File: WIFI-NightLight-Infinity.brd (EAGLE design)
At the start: 49.2 x 44.4 mm, 34 parts, among them CN1 PBS-3-VERTICAL, CN2 PBS-2-VERTICAL, CN5 PBS-2-VERTICAL, CN6 PBS-2-VERTICAL, CN7 PBS-4-VERTICAL, IC3 MC34063AD, IC4 DS1307Z, M1 ESP8266-12F, Q1 32.768K

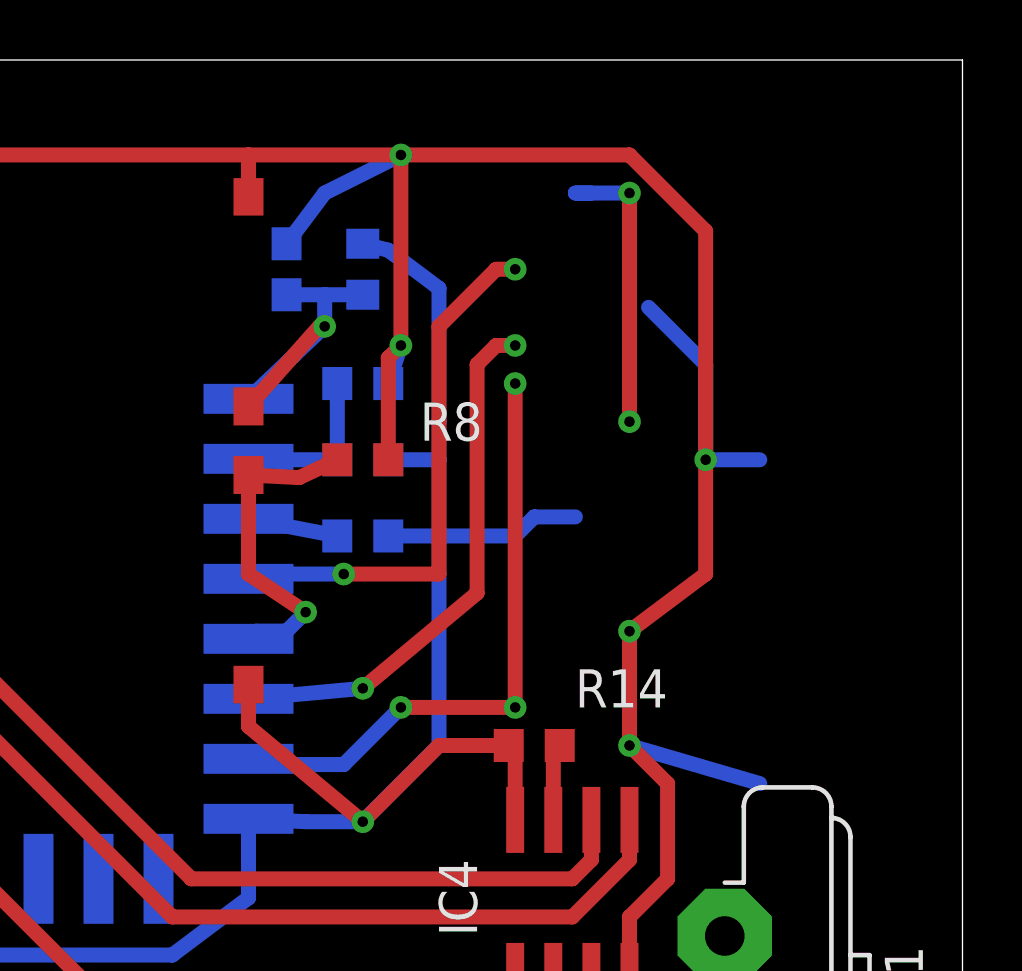
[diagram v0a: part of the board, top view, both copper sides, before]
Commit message: transistors were aaded
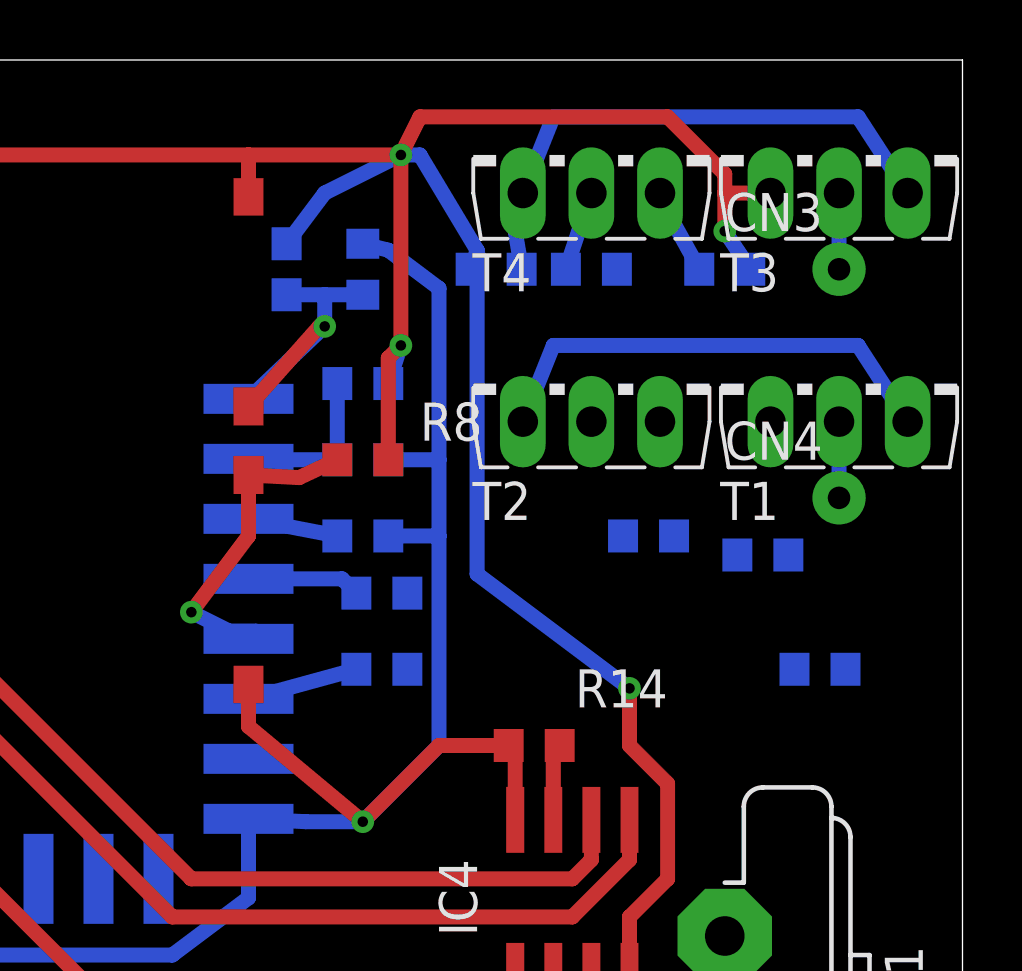
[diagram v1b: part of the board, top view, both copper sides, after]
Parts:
- added CN3, CN4: (no value), pls:PBS-1-VERTICAL
- added R15, R16, R17, R18, R19, R20, R21, R22: 100K, eagle-ltspice:R0603
- added T1, T2, T3, T4: (no value), transistor:TO126V
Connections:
- net SCK renamed LED_KEY_B
- removed net N$27: M1.G16
- removed net RCK: M1.G12
- new net LED_KEY_G: M1.G12, R19.2
- new net LED_KEY_R: M1.G16, R15.2
- new net N$10: R17.1, T4.2
- new net N$11: R19.1, R20.2, T2.3
- new net N$12: CN3.P$1, T3.2
- new net N$13: R21.2, T1.3, T2.1
- new net N$14: R22.1, T2.2
- new net N$15: CN4.P$1, T1.2
- new net N$8: R15.1, R18.2, T4.3
- new net N$9: R16.2, T3.3, T4.1
- net +5V: now also R17.2, R22.2
- net GND: now also R16.1, R18.1, R20.1, R21.1, T1.1, T3.1
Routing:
- net LED_KEY_B: track 20.5 -> 0.00 mm, vias 3 -> 0
- net N$9: track 0.00 -> 18.5 mm
- net N$27: track 18.0 -> 0.00 mm, vias 2 -> 0
- net RCK: track 17.9 -> 0.00 mm, vias 2 -> 0
- net N$13: track 0.00 -> 15.9 mm
- net +3V3: track 135.1 -> 120.4 mm, vias 5 -> 3
- net LED_KEY_R: track 0.00 -> 3.79 mm
- net LED_KEY_G: track 0.00 -> 3.73 mm
- net N$8: track 0.00 -> 3.46 mm
- net N$10: track 0.00 -> 2.68 mm
- net N$15: track 0.00 -> 2.54 mm
- net N$12: track 0.00 -> 2.54 mm
- net GND: track 262.9 -> 262.5 mm, vias 9 -> 8
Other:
- board text added: "Polyakov Konstantin Russia, Yeysk, 2018-09-16, v0.1 rev1"
- board text removed: "16 Channels 1"
- board text removed: "Polyakov Konstantin Russia, Yeysk, 2018-04-26, v0.3 rev1"

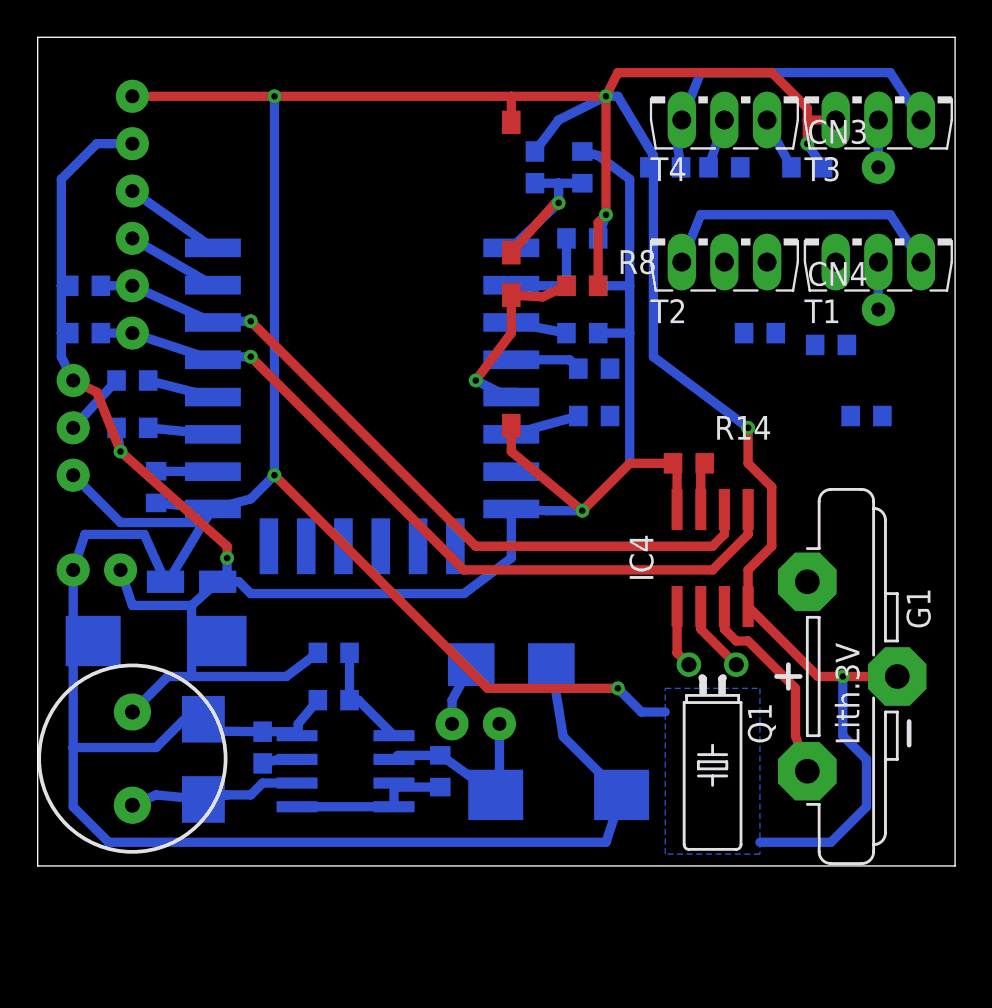
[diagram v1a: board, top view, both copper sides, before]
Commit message: Scheme for all led-channels have done
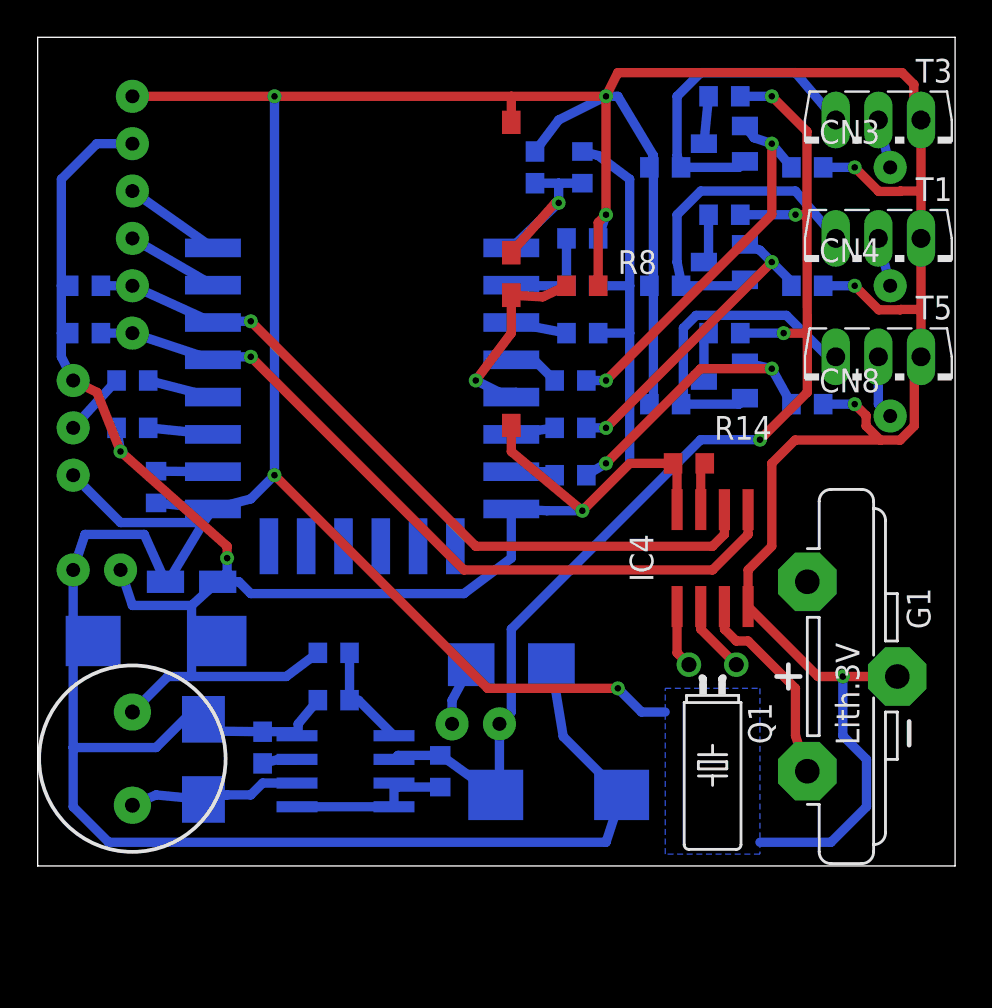
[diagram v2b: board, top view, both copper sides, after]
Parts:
- added CN8: (no value), pls:PBS-1-VERTICAL
- added R23, R24, R25, R26: 100K, eagle-ltspice:R0603
- added T5: (no value), transistor:TO126V
- added T6: BC847, transistor:SOT23
- T2, T4: value (none) -> BC847; device transistor:TO126V -> transistor:SOT23
- moved R21 12.9 mm to (33.7, 31.1), turned to 180 degrees
- moved R22 6.63 mm to (36.8, 34.9), turned to 180 degrees
- moved R17 3.81 mm to (36.8, 41.3)
- moved R20 3.42 mm to (41.3, 31.1), turned to 0 degrees
- moved T3 2.54 mm to (45.1, 38.7), turned to 180 degrees
- moved T4 2.54 mm to (36.8, 38.7), flipped to the bottom, turned to 270 degrees
- moved R15 1.42 mm to (28.6, 26.0)
- moved CN4 1.42 mm to (45.7, 31.1)
- moved R19 1.42 mm to (28.6, 23.5)
- moved T1 1.27 mm to (45.1, 32.4), turned to 180 degrees
- moved T2 1.27 mm to (36.8, 32.4), flipped to the bottom, turned to 270 degrees
- moved CN3 0.63 mm to (45.7, 37.5)
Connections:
- new net N$16: R23.1, R24.2, T6.1
- new net N$17: R25.2, T5.3, T6.2
- new net N$18: R26.1, T6.3
- new net N$19: CN8.P$1, T5.2
- net +5V: now also R26.2
- net GND: now also R24.1, R25.1, T5.1
- net LED_KEY_B: now also R23.2
- net N$10: now also T4.3; no longer T4.2
- net N$11: now also T2.1; no longer T2.3
- net N$13: now also T2.2; no longer T2.1
- net N$14: now also T2.3; no longer T2.2
- net N$8: now also T4.1; no longer T4.3
- net N$9: now also T4.2; no longer T4.1
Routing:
- net +5V: track 10.3 -> 62.3 mm, vias 0 -> 4
- net GND: track 262.5 -> 299.9 mm, vias 8 -> 9
- net N$8: track 3.46 -> 20.9 mm, vias 0 -> 2
- net N$11: track 0.00 -> 17.4 mm, vias 0 -> 2
- net N$17: track 0.00 -> 17.1 mm
- net N$16: track 0.00 -> 15.9 mm, vias 0 -> 2
- net N$19: track 0.00 -> 3.44 mm
- net N$18: track 0.00 -> 2.64 mm
- net N$14: track 0.00 -> 2.61 mm
- net LED_KEY_B: track 0.00 -> 2.36 mm
- net N$13: track 15.9 -> 17.6 mm
- net LED_KEY_G: track 3.73 -> 2.35 mm
- net LED_KEY_R: track 3.79 -> 2.78 mm
- net N$9: track 18.5 -> 17.6 mm

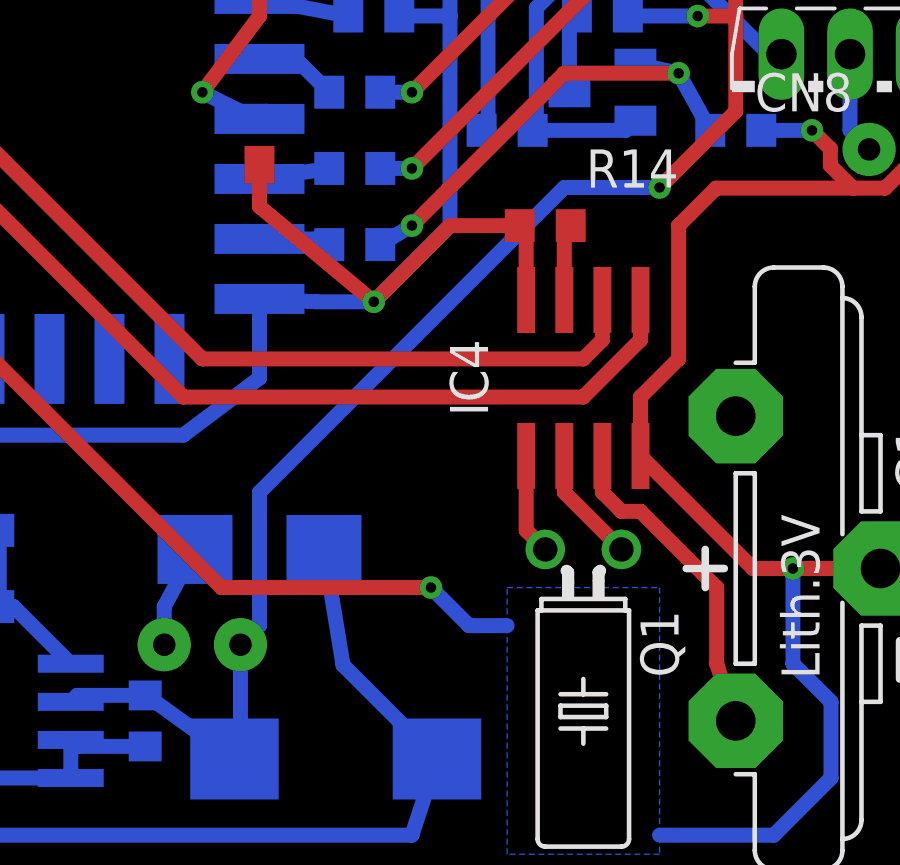
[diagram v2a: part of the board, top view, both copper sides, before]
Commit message: Resistor was added for plus of LED-strip
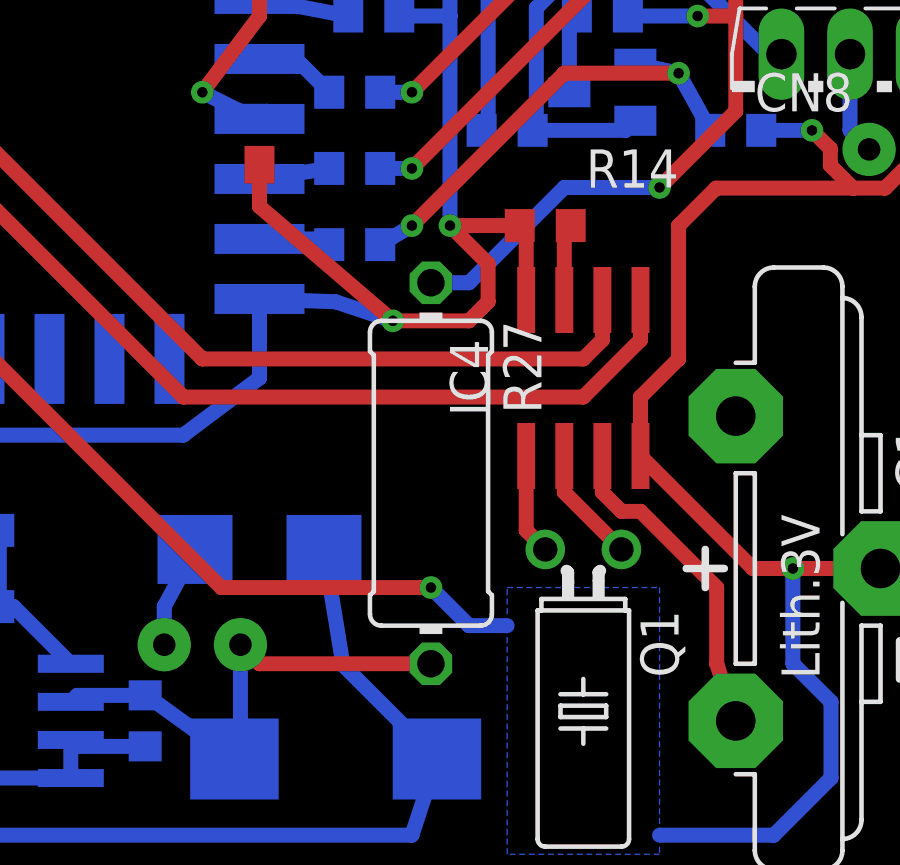
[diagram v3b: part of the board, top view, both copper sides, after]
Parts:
- added R27: (no value), resistor:0411/12
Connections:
- new net N$21: R17.2, R22.2, R26.2, R27.1
- net +5V: now also R27.2; no longer R17.2, R22.2, R26.2
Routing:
- net +5V: track 62.3 -> 17.0 mm, vias 4 -> 0
- net N$21: track 0.00 -> 38.0 mm, vias 0 -> 4
- net +3V3: track 120.4 -> 121.3 mm, vias 3 -> 4
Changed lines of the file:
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@@
 </element>
 <element name="CN8" library="pls" package="PBS-1-VERTICAL" value="" x="45.72" y="24.13"/>
+<element name="R27" library="resistor" library_urn="urn:adsk.eagle:library:348" package="0411/12" package3d_urn="urn:adsk.eagle:package:26091/1" value="" x="31.115" y="13.335" rot="R270"/>
 </elements>
 <signals>
@@
 <wire x1="22.86" y1="14.605" x2="25.4" y2="16.51" width="0.5" layer="16"/>
 <wire x1="25.4" y1="16.51" x2="25.4" y2="19.145" width="0.5" layer="16"/>
-<wire x1="25.4" y1="19.145" x2="27.305" y2="19.05" width="0.5" layer="16"/>
-<wire x1="27.305" y1="19.05" x2="29.21" y2="19.05" width="0.5" layer="16"/>
-<via x="29.21" y="19.05" extent="1-16" drill="0.35"/>
+<wire x1="25.4" y1="19.145" x2="27.94" y2="19.05" width="0.5" layer="16"/>
+<wire x1="27.94" y1="19.05" x2="29.845" y2="18.415" width="0.5" layer="16"/>
+<via x="29.845" y="18.415" extent="1-16" drill="0.35"/>
 <wire x1="29.21" y1="38.315" x2="30.06" y2="38.1" width="0.5" layer="16"/>
 <wire x1="30.06" y1="38.1" x2="31.75" y2="36.83" width="0.5" layer="16"/>
@@
 <wire x1="25.4" y1="23.622" x2="25.4" y2="22.225" width="0.5" layer="1"/>
 <wire x1="30.06" y1="31.115" x2="31.75" y2="31.115" width="0.5" layer="16"/>
-<wire x1="31.75" y1="21.59" x2="29.21" y2="19.05" width="0.5" layer="16"/>
-<wire x1="25.4" y1="22.225" x2="29.21" y2="19.05" width="0.5" layer="1"/>
+<wire x1="25.4" y1="22.225" x2="29.845" y2="18.415" width="0.5" layer="1"/>
 <contactref element="IC4" pad="8"/>
 <contactref element="R13" pad="2"/>
@@
 <wire x1="10.16" y1="17.145" x2="4.445" y2="22.225" width="0.5" layer="1"/>
 <wire x1="34.29" y1="21.375" x2="34.29" y2="19.11" width="0.5" layer="1"/>
-<wire x1="29.21" y1="19.05" x2="31.75" y2="21.59" width="0.5" layer="1"/>
-<wire x1="31.75" y1="21.59" x2="34.075" y2="21.59" width="0.5" layer="1"/>
 <wire x1="34.075" y1="21.59" x2="34.29" y2="21.375" width="0.5" layer="1"/>
 <wire x1="30.06" y1="28.575" x2="31.75" y2="28.575" width="0.5" layer="16"/>
+<via x="31.75" y="21.59" extent="1-16" drill="0.35"/>
+<wire x1="31.75" y1="21.59" x2="34.075" y2="21.59" width="0.5" layer="1"/>
+<wire x1="32.385" y1="18.415" x2="33.02" y2="19.05" width="0.5" layer="1"/>
+<wire x1="33.02" y1="19.05" x2="33.02" y2="20.32" width="0.5" layer="1"/>
+<wire x1="33.02" y1="20.32" x2="31.75" y2="21.59" width="0.5" layer="1"/>
+<wire x1="29.845" y1="18.415" x2="32.385" y2="18.415" width="0.5" layer="1"/>
 </signal>
 <signal name="N$1">
@@
 <wire x1="24.565" y1="3.81" x2="21.485" y2="6.035" width="0.5" layer="16"/>
 <wire x1="21.485" y1="6.035" x2="21.59" y2="5.93" width="0.5" layer="16"/>
-<contactref element="R17" pad="2"/>
-<contactref element="R22" pad="2"/>
-<wire x1="37.68" y1="41.275" x2="39.37" y2="41.275" width="0.5" layer="16"/>
-<via x="39.37" y="41.275" extent="1-16" drill="0.35"/>
-<wire x1="37.68" y1="34.925" x2="40.64" y2="34.925" width="0.5" layer="16"/>
-<via x="40.64" y="34.925" extent="1-16" drill="0.35"/>
-<wire x1="39.37" y1="41.275" x2="41.2576" y2="39.3874" width="0.5" layer="1"/>
-<wire x1="41.2576" y1="39.3874" x2="41.2576" y2="34.925" width="0.5" layer="1"/>
-<wire x1="41.275" y1="28.575" x2="41.2576" y2="34.925" width="0.5" layer="1"/>
-<wire x1="40.64" y1="34.925" x2="41.2576" y2="34.925" width="0.5" layer="1"/>
-<contactref element="R26" pad="2"/>
-<wire x1="37.68" y1="28.575" x2="40.005" y2="28.575" width="0.5" layer="16"/>
-<via x="40.005" y="28.575" extent="1-16" drill="0.35"/>
-<wire x1="40.005" y1="28.575" x2="41.275" y2="28.575" width="0.5" layer="1"/>
-<wire x1="24.765" y1="7.62" x2="25.4" y2="8.255" width="0.5" layer="16"/>
-<wire x1="25.4" y1="8.255" x2="25.4" y2="12.7" width="0.5" layer="16"/>
-<wire x1="25.4" y1="12.7" x2="35.56" y2="22.86" width="0.5" layer="16"/>
-<wire x1="35.56" y1="22.86" x2="38.735" y2="22.86" width="0.5" layer="16"/>
-<via x="38.735" y="22.86" extent="1-16" drill="0.35"/>
-<wire x1="38.735" y1="22.86" x2="41.275" y2="25.4" width="0.5" layer="1"/>
-<wire x1="41.275" y1="25.4" x2="41.275" y2="28.575" width="0.5" layer="1"/>
+<contactref element="R27" pad="2"/>
+<wire x1="31.115" y1="6.985" x2="25.4" y2="6.985" width="0.5" layer="1"/>
+<wire x1="25.4" y1="6.985" x2="24.765" y2="7.62" width="0.5" layer="1"/>
 </signal>
 <signal name="N$32">
@@
 <wire x1="45.085" y1="24.765" x2="45.085" y2="27.305" width="0.5" layer="16"/>
 </signal>
+<signal name="N$21">
+<contactref element="R26" pad="2"/>
+<contactref element="R22" pad="2"/>
+<contactref element="R17" pad="2"/>
+<contactref element="R27" pad="1"/>
+<via x="39.37" y="41.275" extent="1-16" drill="0.35"/>
+<via x="40.64" y="34.925" extent="1-16" drill="0.35"/>
+<wire x1="39.37" y1="41.275" x2="41.2576" y2="39.3874" width="0.5" layer="1"/>
+<wire x1="41.2576" y1="39.3874" x2="41.2576" y2="34.925" width="0.5" layer="1"/>
+<wire x1="41.275" y1="28.575" x2="41.2576" y2="34.925" width="0.5" layer="1"/>
+<via x="40.005" y="28.575" extent="1-16" drill="0.35"/>
+<wire x1="40.005" y1="28.575" x2="41.275" y2="28.575" width="0.5" layer="1"/>
+<wire x1="38.735" y1="22.86" x2="35.56" y2="22.86" width="0.5" layer="16"/>
+<via x="38.735" y="22.86" extent="1-16" drill="0.35"/>
+<wire x1="38.735" y1="22.86" x2="41.275" y2="25.4" width="0.5" layer="1"/>
+<wire x1="41.275" y1="25.4" x2="41.275" y2="28.575" width="0.5" layer="1"/>
+<wire x1="40.64" y1="34.925" x2="41.2576" y2="34.925" width="0.5" layer="1"/>
+<wire x1="37.68" y1="34.925" x2="40.64" y2="34.925" width="0.5" layer="16"/>
+<wire x1="37.68" y1="41.275" x2="39.37" y2="41.275" width="0.5" layer="16"/>
+<wire x1="37.68" y1="28.575" x2="40.005" y2="28.575" width="0.5" layer="16"/>
+<wire x1="35.56" y1="22.86" x2="32.385" y2="19.685" width="0.5" layer="16"/>
+<wire x1="32.385" y1="19.685" x2="31.115" y2="19.685" width="0.5" layer="16"/>
+</signal>
 </signals>
